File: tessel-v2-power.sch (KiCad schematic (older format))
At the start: 51 parts, among them Q601 MMSS8550, U601 AAT4610, U602 AAT4610, U603 AP3417C, U604 AP3417C, U605 AP3418

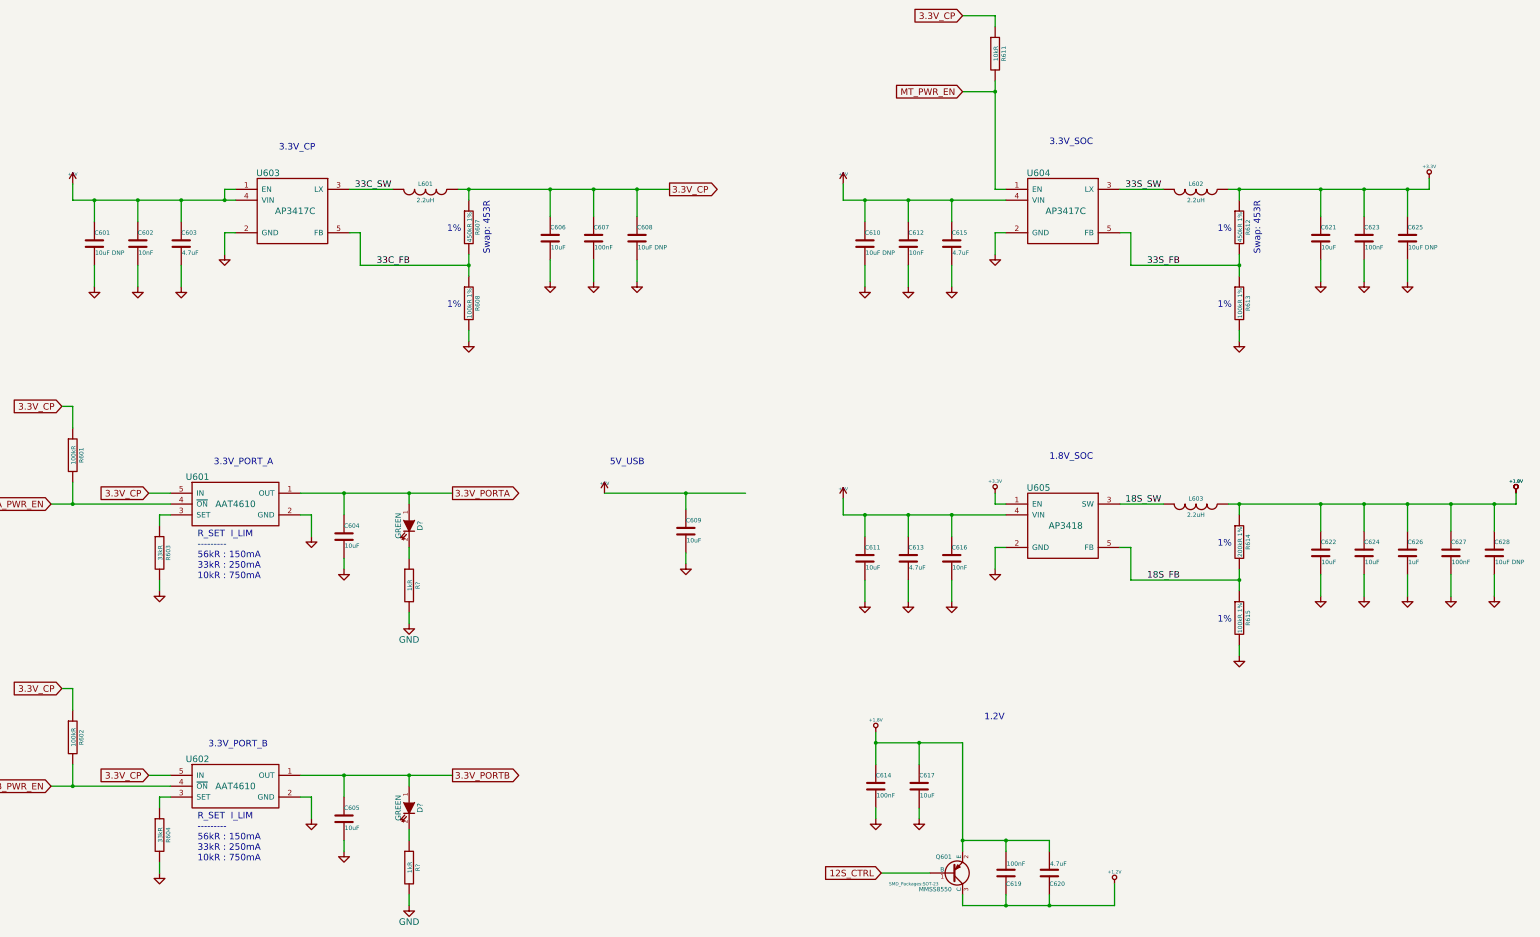
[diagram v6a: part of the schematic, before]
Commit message: reset annotation
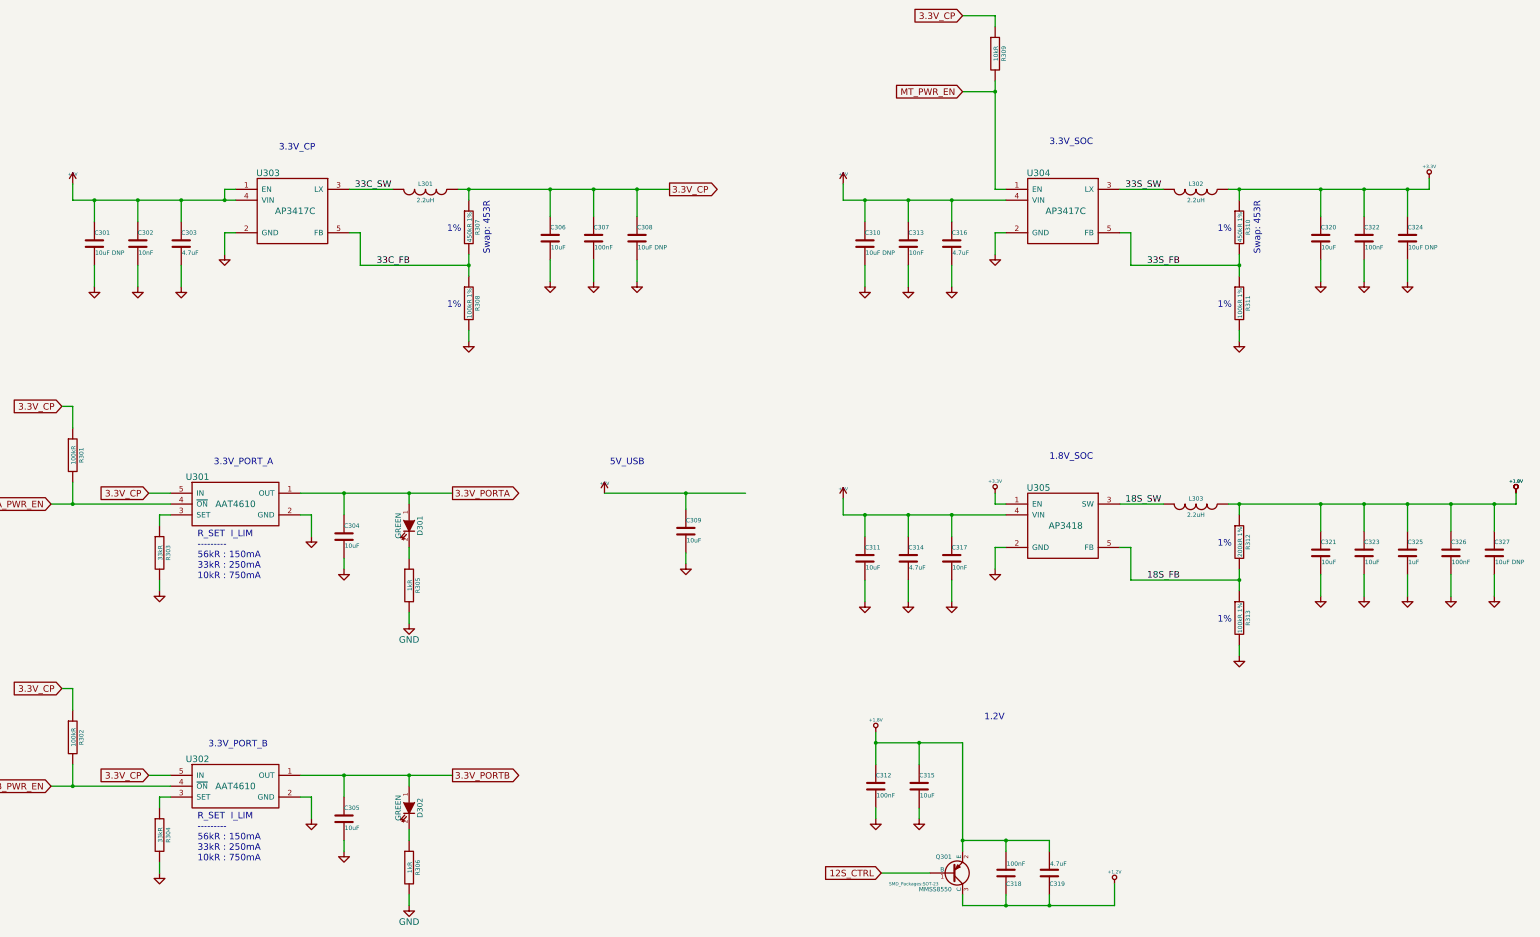
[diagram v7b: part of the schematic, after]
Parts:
- gave numbers to parts that had none: 4
- renumbered C601 to C301, C602 to C302, C603 to C303, C604 to C304, C605 to C305, C606 to C306, C607 to C307, C608 to C308, C609 to C309, C610 to C310, C611 to C311, C614 to C312, C612 to C313, C613 to C314, C617 to C315, C615 to C316, C616 to C317, C619 to C318, C620 to C319, C621 to C320, C622 to C321, C623 to C322, C624 to C323, C625 to C324, C626 to C325, C627 to C326, C628 to C327, L601 to L301, L602 to L302, L603 to L303, Q601 to Q301, R601 to R301, R602 to R302, R603 to R303, R604 to R304, R607 to R307, R608 to R308, R611 to R309, R612 to R310, R613 to R311, R614 to R312, R615 to R313, U601 to U301, U602 to U302, U603 to U303, U604 to U304, U605 to U305

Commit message: annotation did not take?
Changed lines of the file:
@@
 Connection ~ 9300 7900
 Wire Wire Line
-	9300 7800 9300 7900
-Wire Wire Line
-	9300 7900 9300 8100
+	9300 7800 9300 8100
 Wire Wire Line
 	10400 5700 10400 5600
@@
 Connection ~ 3300 2900
 Wire Wire Line
-	3300 2800 3300 2900
+	3300 2900 3300 2800
 Connection ~ 1900 8300
 Wire Wire Line
@@
 Connection ~ 10000 5800
 Wire Wire Line
-	10000 6000 10000 5800
+	10000 5800 10000 6000
 Wire Wire Line
 	10400 5700 10500 5700
@@
 	9600 5800 9600 6000
 Wire Wire Line
-	9000 5800 9200 5800
-Wire Wire Line
-	9200 5800 9600 5800
-Wire Wire Line
-	9600 5800 10000 5800
-Wire Wire Line
-	10000 5800 10500 5800
+	9000 5800 10500 5800
 Wire Wire Line
 	9200 6000 9200 5800
@@
 	12650 5700 12650 5800
 Wire Wire Line
-	12550 5700 12650 5700
-Wire Wire Line
-	12650 5700 13400 5700
-Wire Wire Line
-	13400 5700 13800 5700
-Wire Wire Line
-	13800 5700 14200 5700
-Wire Wire Line
-	14200 5700 14600 5700
-Wire Wire Line
-	14600 5700 15000 5700
-Wire Wire Line
-	15000 5700 15200 5700
+	12550 5700 15200 5700
 Connection ~ 12650 6400
 Wire Wire Line
-	12650 6300 12650 6400
-Wire Wire Line
-	12650 6400 12650 6500
+	12650 6300 12650 6500
 Wire Wire Line
 	14400 2800 14400 2700
@@
 Connection ~ 10000 2900
 Wire Wire Line
-	10000 3100 10000 2900
+	10000 2900 10000 3100
 Wire Wire Line
 	10400 2800 10500 2800
@@
 Connection ~ 10400 1900
 Wire Wire Line
-	10400 1800 10400 1900
-Wire Wire Line
-	10400 1900 10400 2800
+	10400 1800 10400 2800
 Wire Wire Line
 	10100 1900 10400 1900
@@
 	9600 2900 9600 3100
 Wire Wire Line
-	9000 2900 9200 2900
-Wire Wire Line
-	9200 2900 9600 2900
-Wire Wire Line
-	9600 2900 10000 2900
-Wire Wire Line
-	10000 2900 10500 2900
+	9000 2900 10500 2900
 Wire Wire Line
 	9200 3100 9200 2900
@@
 	12650 2800 12650 2900
 Wire Wire Line
-	12550 2800 12650 2800
-Wire Wire Line
-	12650 2800 13400 2800
-Wire Wire Line
-	13400 2800 13800 2800
-Wire Wire Line
-	13800 2800 14200 2800
-Wire Wire Line
-	14200 2800 14400 2800
+	12550 2800 14400 2800
 Connection ~ 12650 3500
 Wire Wire Line
-	12650 3400 12650 3500
-Wire Wire Line
-	12650 3500 12650 3600
+	12650 3400 12650 3600
 Wire Wire Line
 	3300 3200 3300 3400
@@
 Connection ~ 2900 2900
 Wire Wire Line
-	2900 3100 2900 2900
+	2900 2900 2900 3100
 Connection ~ 4400 8200
 Wire Wire Line
@@
 	2600 8200 2800 8200
 Wire Wire Line
-	4000 8200 4400 8200
-Wire Wire Line
-	4400 8200 5400 8200
-Wire Wire Line
-	1700 8300 1900 8300
-Wire Wire Line
-	1900 8300 2800 8300
+	4000 8200 5400 8200
+Wire Wire Line
+	1700 8300 2800 8300
 Connection ~ 4400 5600
 Wire Wire Line
@@
 	10500 8800 10500 8900
 Wire Wire Line
-	10100 8800 10500 8800
-Wire Wire Line
-	10500 8800 10900 8800
-Wire Wire Line
-	10100 9400 10500 9400
-Wire Wire Line
-	10500 9400 10900 9400
-Wire Wire Line
-	10900 9400 11500 9400
+	10100 8800 10900 8800
+Wire Wire Line
+	10100 9400 11500 9400
 Wire Wire Line
 	10500 9300 10500 9400
@@
 	4100 5800 4100 6000
 Wire Wire Line
-	9300 7900 9700 7900
-Wire Wire Line
-	9700 7900 10100 7900
-Wire Wire Line
-	10100 7900 10100 8800
-Wire Wire Line
-	10100 8800 10100 8900
+	9300 7900 10100 7900
+Wire Wire Line
+	10100 7900 10100 8900
 Wire Wire Line
 	9800 9100 9350 9100
@@
 	2600 5600 2800 5600
 Wire Wire Line
-	4000 5600 4400 5600
-Wire Wire Line
-	4400 5600 5400 5600
-Wire Wire Line
-	1700 5700 1900 5700
-Wire Wire Line
-	1900 5700 2800 5700
+	4000 5600 5400 5600
+Wire Wire Line
+	1700 5700 2800 5700
 Connection ~ 2100 2900
 Connection ~ 2500 2900
@@
 	2500 2900 2500 3100
 Wire Wire Line
-	1900 2900 2100 2900
-Wire Wire Line
-	2100 2900 2500 2900
-Wire Wire Line
-	2500 2900 2900 2900
-Wire Wire Line
-	2900 2900 3300 2900
-Wire Wire Line
-	3300 2900 3400 2900
+	1900 2900 3400 2900
 Wire Wire Line
 	2100 3100 2100 2900
@@
 	5550 2800 5550 2900
 Wire Wire Line
-	5450 2800 5550 2800
-Wire Wire Line
-	5550 2800 6300 2800
-Wire Wire Line
-	6300 2800 6700 2800
-Wire Wire Line
-	6700 2800 7100 2800
-Wire Wire Line
-	7100 2800 7400 2800
+	5450 2800 7400 2800
 Connection ~ 5550 3500
 Wire Wire Line
-	5550 3400 5550 3500
-Wire Wire Line
-	5550 3500 5550 3600
+	5550 3400 5550 3600
 Wire Wire Line
 	7550 6150 7550 6250
@@
 	7550 5750 7550 5600
 Wire Wire Line
-	6800 5600 7550 5600
-Wire Wire Line
-	7550 5600 8100 5600
+	6800 5600 8100 5600
 $Comp
 L GND #PWR325
